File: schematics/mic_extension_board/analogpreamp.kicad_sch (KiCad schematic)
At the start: 61 parts, among them J1 XLR3, J3 Aux In, J4 Conn_01x02_Pin, J7 XLR3, J8 XLR3, U1 TL074, U4 NE5534, U9 TL074

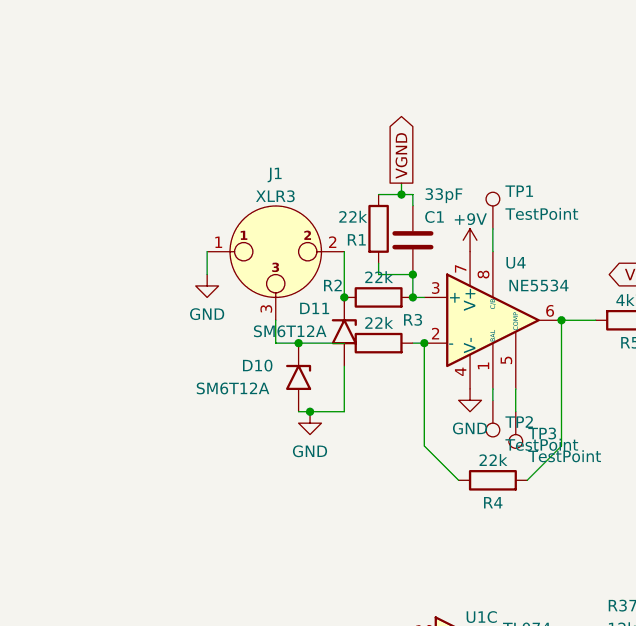
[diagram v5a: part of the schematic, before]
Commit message: added decoupling caps at mic input
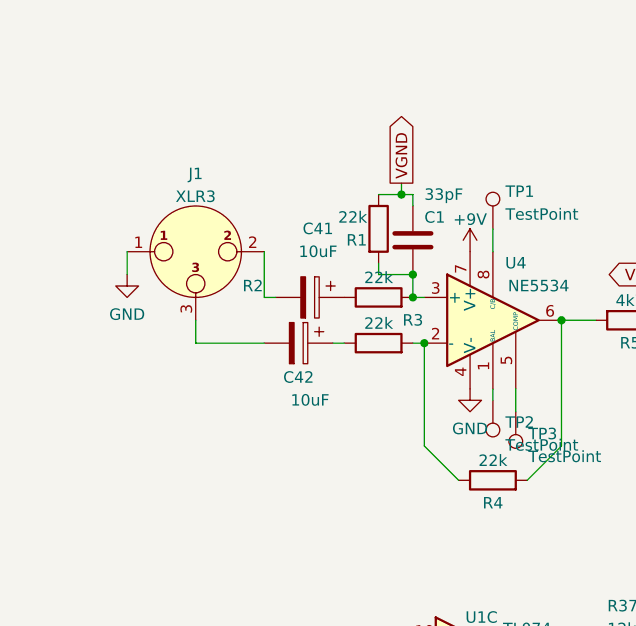
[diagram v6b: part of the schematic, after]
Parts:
- removed D10, D11: SM6T12A, Diode_SMD:D_SMB, symbol Diode:SM6T12A
- added C41, C42: 10uF, Capacitor_SMD:CP_Elec_4x4.5, symbol Device:C_Polarized
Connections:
- net at R2.1: now also C41.1; no longer J1.2
- net at J1.3: now also C42.2; no longer R3.1
- new net: C41.2, J1.2
- new net: C42.1, R3.1
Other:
- moved on the sheet: J1
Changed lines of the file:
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@@
   (junction (at 41.91 111.76) (diameter 0) (color 0 0 0 0)
   )
-  (junction (at 45.72 67.31) (diameter 0) (color 0 0 0 0)
-  )
   (junction (at 57.15 50.8) (diameter 0) (color 0 0 0 0)
   )
   (junction (at 118.11 111.76) (diameter 0) (color 0 0 0 0)
   )
-  (junction (at 50.8 62.23) (diameter 0) (color 0 0 0 0)
-  )
   (junction (at 95.25 69.85) (diameter 0) (color 0 0 0 0)
   )
@@
   (junction (at 90.17 69.85) (diameter 0) (color 0 0 0 0)
   )
-  (junction (at 46.99 74.93) (diameter 0) (color 0 0 0 0)
-  )
   (junction (at 86.36 101.6) (diameter 0) (color 0 0 0 0)
   )
@@
     (stroke (width 0) (type default))
   )
-  (wire (pts (xy 50.8 57.15) (xy 50.8 62.23))
+  (wire (pts (xy 41.91 57.15) (xy 41.91 62.23))
     (stroke (width 0) (type default))
   )
@@
     (stroke (width 0) (type default))
   )
-  (wire (pts (xy 50.8 69.85) (xy 50.8 74.93))
-    (stroke (width 0) (type default))
-  )
   (wire (pts (xy 123.19 93.98) (xy 129.54 93.98))
     (stroke (width 0) (type default))
@@
     (stroke (width 0) (type default))
   )
-  (wire (pts (xy 46.99 74.93) (xy 45.72 74.93))
-    (stroke (width 0) (type default))
-  )
   (wire (pts (xy 86.36 101.6) (xy 90.17 101.6))
     (stroke (width 0) (type default))
@@
     (stroke (width 0) (type default))
   )
+  (wire (pts (xy 41.91 62.23) (xy 43.18 62.23))
+    (stroke (width 0) (type default))
+  )
   (wire (pts (xy 57.15 148.59) (xy 57.15 154.94))
     (stroke (width 0) (type default))
@@
     (stroke (width 0) (type default))
   )
-  (wire (pts (xy 45.72 67.31) (xy 50.8 67.31))
+  (wire (pts (xy 34.29 67.31) (xy 41.91 67.31))
     (stroke (width 0) (type default))
   )
@@
     (stroke (width 0) (type default))
   )
-  (wire (pts (xy 43.18 67.31) (xy 45.72 67.31))
-    (stroke (width 0) (type default))
-  )
   (wire (pts (xy 40.64 134.62) (xy 35.56 134.62))
     (stroke (width 0) (type default))
@@
     (stroke (width 0) (type default))
   )
+  (wire (pts (xy 49.53 67.31) (xy 50.8 67.31))
+    (stroke (width 0) (type default))
+  )
   (wire (pts (xy 49.53 134.62) (xy 50.8 134.62))
     (stroke (width 0) (type default))
@@
     (stroke (width 0) (type default))
   )
-  (wire (pts (xy 43.18 64.77) (xy 43.18 67.31))
+  (wire (pts (xy 34.29 64.77) (xy 34.29 67.31))
     (stroke (width 0) (type default))
   )
@@
     (stroke (width 0) (type default))
   )
-  (wire (pts (xy 50.8 74.93) (xy 46.99 74.93))
-    (stroke (width 0) (type default))
-  )
   (wire (pts (xy 58.42 62.23) (xy 59.69 62.23))
     (stroke (width 0) (type default))
@@
     (stroke (width 0) (type default))
   )
-  (wire (pts (xy 35.56 57.15) (xy 35.56 59.69))
+  (wire (pts (xy 26.67 57.15) (xy 26.67 59.69))
     (stroke (width 0) (type default))
   )
@@
   (symbol (lib_id "Device:R") (at 54.61 62.23 90) (unit 1)
     (in_bom yes) (on_board yes) (dnp no)
-    (property "Reference" "R2" (at 49.53 60.96 90)
+    (property "Reference" "R2" (at 40.64 60.96 90)
       (effects (font (size 1.27 1.27)))
     )
@@
     )
   )
-  (symbol (lib_id "Connector:XLR3") (at 43.18 57.15 0) (unit 1)
-    (in_bom yes) (on_board yes) (dnp no) (fields_autoplaced)
-    (property "Reference" "J1" (at 43.18 48.4972 0)
-      (effects (font (size 1.27 1.27)))
-    )
-    (property "Value" "XLR3" (at 43.18 51.0341 0)
-      (effects (font (size 1.27 1.27)))
-    )
-    (property "Footprint" "Connector_PinHeader_2.54mm:PinHeader_1x03_P2.54mm_Vertical" (at 43.18 57.15 0)
-      (effects (font (size 1.27 1.27)) hide)
-    )
-    (property "Datasheet" " ~" (at 43.18 57.15 0)
+  (symbol (lib_id "Connector:XLR3") (at 34.29 57.15 0) (unit 1)
+    (in_bom yes) (on_board yes) (dnp no) (fields_autoplaced)
+    (property "Reference" "J1" (at 34.29 48.4972 0)
+      (effects (font (size 1.27 1.27)))
+    )
+    (property "Value" "XLR3" (at 34.29 51.0341 0)
+      (effects (font (size 1.27 1.27)))
+    )
+    (property "Footprint" "Connector_PinHeader_2.54mm:PinHeader_1x03_P2.54mm_Vertical" (at 34.29 57.15 0)
+      (effects (font (size 1.27 1.27)) hide)
+    )
+    (property "Datasheet" " ~" (at 34.29 57.15 0)
       (effects (font (size 1.27 1.27)) hide)
     )
@@
     )
   )
-  (symbol (lib_id "Diode:SM6T12A") (at 50.8 66.04 270) (unit 1)
-    (in_bom yes) (on_board yes) (dnp no)
-    (property "Reference" "D11" (at 45.72 63.5 90)
-      (effects (font (size 1.27 1.27)) (justify left))
-    )
-    (property "Value" "SM6T12A" (at 40.64 66.04 90)
-      (effects (font (size 1.27 1.27)) (justify left))
-    )
-    (property "Footprint" "Diode_SMD:D_SMB" (at 45.72 66.04 0)
-      (effects (font (size 1.27 1.27)) hide)
-    )
-    (property "Datasheet" "https://www.st.com/resource/en/datasheet/sm6t.pdf" (at 50.8 64.77 0)
-      (effects (font (size 1.27 1.27)) hide)
-    )
-    (pin "2")
-    (pin "1")
-    (instances
-      (project "mic_extension_board"
-        (path "/e63e39d7-6ac0-4ffd-8aa3-1841a4541b55/9b4677b6-5618-4dd2-a345-e4ce8cf01c2f"
-          (reference "D11") (unit 1)
-        )
-      )
-    )
-  )
   (symbol (lib_id "Device:R") (at 217.17 95.25 0) (mirror y) (unit 1)
     (in_bom yes) (on_board yes) (dnp no)
@@
         (path "/e63e39d7-6ac0-4ffd-8aa3-1841a4541b55/9b4677b6-5618-4dd2-a345-e4ce8cf01c2f"
           (reference "U9") (unit 2)
-        )
-      )
-    )
-  )
-  (symbol (lib_id "power:GND") (at 46.99 74.93 0) (unit 1)
-    (in_bom yes) (on_board yes) (dnp no) (fields_autoplaced)
-    (property "Reference" "#PWR051" (at 46.99 81.28 0)
-      (effects (font (size 1.27 1.27)) hide)
-    )
-    (property "Value" "GND" (at 46.99 79.3734 0)
-      (effects (font (size 1.27 1.27)))
-    )
-    (property "Footprint" "" (at 46.99 74.93 0)
-      (effects (font (size 1.27 1.27)) hide)
-    )
-    (property "Datasheet" "" (at 46.99 74.93 0)
-      (effects (font (size 1.27 1.27)) hide)
-    )
-    (pin "1")
-    (instances
-      (project "mic_extension_board"
-        (path "/e63e39d7-6ac0-4ffd-8aa3-1841a4541b55/9b4677b6-5618-4dd2-a345-e4ce8cf01c2f"
-          (reference "#PWR051") (unit 1)
         )
       )
@@
     )
   )
+  (symbol (lib_id "Device:C_Polarized") (at 45.72 67.31 270) (unit 1)
+    (in_bom yes) (on_board yes) (dnp no)
+    (property "Reference" "C42" (at 45.72 71.12 90)
+      (effects (font (size 1.27 1.27)))
+    )
+    (property "Value" "10uF" (at 46.99 73.66 90)
+      (effects (font (size 1.27 1.27)))
+    )
+    (property "Footprint" "Capacitor_SMD:CP_Elec_4x4.5" (at 41.91 68.2752 0)
+      (effects (font (size 1.27 1.27)) hide)
+    )
+    (property "Datasheet" "~" (at 45.72 67.31 0)
+      (effects (font (size 1.27 1.27)) hide)
+    )
+    (pin "1")
+    (pin "2")
+    (instances
+      (project "mic_extension_board"
+        (path "/e63e39d7-6ac0-4ffd-8aa3-1841a4541b55/9b4677b6-5618-4dd2-a345-e4ce8cf01c2f"
+          (reference "C42") (unit 1)
+        )
+      )
+    )
+  )
   (symbol (lib_id "Amplifier_Operational:TL074") (at 66.04 102.87 0) (unit 3)
     (in_bom yes) (on_board yes) (dnp no)
@@
     )
   )
-  (symbol (lib_id "Diode:SM6T12A") (at 45.72 71.12 270) (unit 1)
-    (in_bom yes) (on_board yes) (dnp no)
-    (property "Reference" "D10" (at 39.37 69.85 90)
-      (effects (font (size 1.27 1.27)) (justify left))
-    )
-    (property "Value" "SM6T12A" (at 34.29 72.39 90)
-      (effects (font (size 1.27 1.27)) (justify left))
-    )
-    (property "Footprint" "Diode_SMD:D_SMB" (at 40.64 71.12 0)
-      (effects (font (size 1.27 1.27)) hide)
-    )
-    (property "Datasheet" "https://www.st.com/resource/en/datasheet/sm6t.pdf" (at 45.72 69.85 0)
-      (effects (font (size 1.27 1.27)) hide)
-    )
-    (pin "2")
-    (pin "1")
-    (instances
-      (project "mic_extension_board"
-        (path "/e63e39d7-6ac0-4ffd-8aa3-1841a4541b55/9b4677b6-5618-4dd2-a345-e4ce8cf01c2f"
-          (reference "D10") (unit 1)
-        )
-      )
-    )
-  )
-  (symbol (lib_id "power:GND") (at 35.56 59.69 0) (unit 1)
-    (in_bom yes) (on_board yes) (dnp no) (fields_autoplaced)
-    (property "Reference" "#PWR01" (at 35.56 66.04 0)
-      (effects (font (size 1.27 1.27)) hide)
-    )
-    (property "Value" "GND" (at 35.56 64.1334 0)
-      (effects (font (size 1.27 1.27)))
-    )
-    (property "Footprint" "" (at 35.56 59.69 0)
-      (effects (font (size 1.27 1.27)) hide)
-    )
-    (property "Datasheet" "" (at 35.56 59.69 0)
+  (symbol (lib_id "power:GND") (at 26.67 59.69 0) (unit 1)
+    (in_bom yes) (on_board yes) (dnp no) (fields_autoplaced)
+    (property "Reference" "#PWR01" (at 26.67 66.04 0)
+      (effects (font (size 1.27 1.27)) hide)
+    )
+    (property "Value" "GND" (at 26.67 64.1334 0)
+      (effects (font (size 1.27 1.27)))
+    )
+    (property "Footprint" "" (at 26.67 59.69 0)
+      (effects (font (size 1.27 1.27)) hide)
+    )
+    (property "Datasheet" "" (at 26.67 59.69 0)
       (effects (font (size 1.27 1.27)) hide)
     )
@@
         )
       )
+    )
+  )
+  (symbol (lib_id "Device:C_Polarized") (at 46.99 62.23 270) (unit 1)
+    (in_bom yes) (on_board yes) (dnp no) (fields_autoplaced)
+    (property "Reference" "C41" (at 47.879 54.61 90)
+      (effects (font (size 1.27 1.27)))
+    )
+    (property "Value" "10uF" (at 47.879 57.15 90)
+      (effects (font (size 1.27 1.27)))
+    )
+    (property "Footprint" "Capacitor_SMD:CP_Elec_4x4.5" (at 43.18 63.1952 0)
+      (effects (font (size 1.27 1.27)) hide)
+    )
+    (property "Datasheet" "~" (at 46.99 62.23 0)
+      (effects (font (size 1.27 1.27)) hide)
+    )
+    (pin "1")
+    (pin "2")
+    (instances
+      (project "mic_extension_board"
+        (path "/e63e39d7-6ac0-4ffd-8aa3-1841a4541b55/9b4677b6-5618-4dd2-a345-e4ce8cf01c2f"
+          (reference "C41") (unit 1)
+        )
+      )
